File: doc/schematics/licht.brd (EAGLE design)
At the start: 49.5 x 40.3 mm, 16 parts, among them Q1 MOSFET-NCHANNELFDS6630A, X1 MKDSN1,5/2-5,08, X2 MKDSN1,5/2-5,08, X3 MKDSN1,5/2-5,08, X4 MKDSN1,5/2-5,08

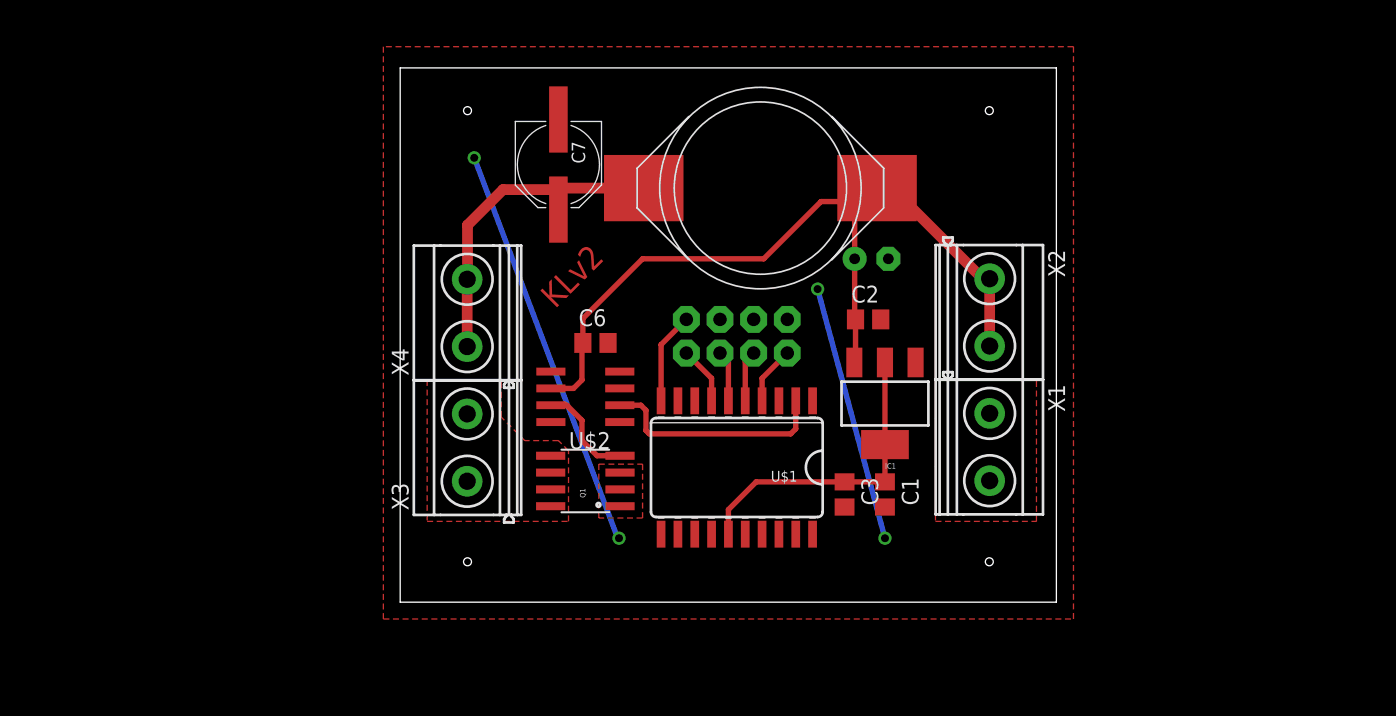
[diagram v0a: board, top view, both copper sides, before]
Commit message: Switched layout and board.
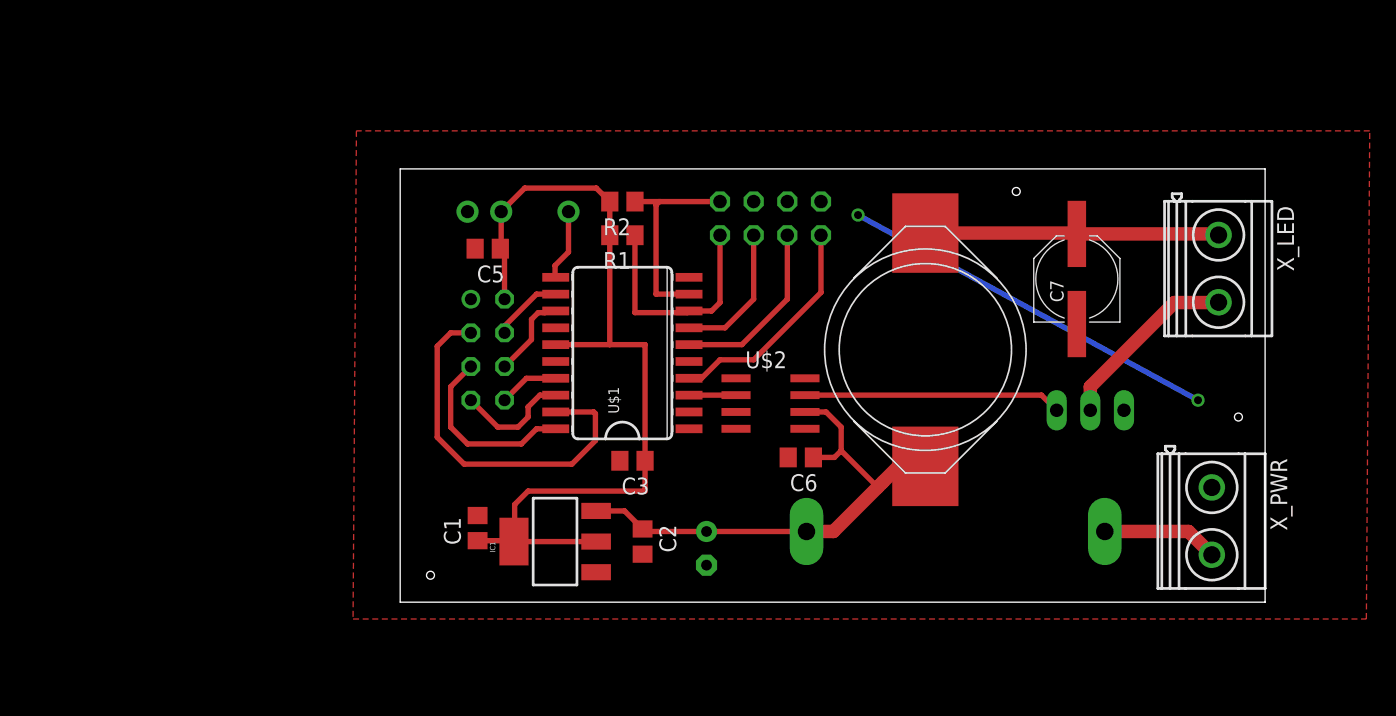
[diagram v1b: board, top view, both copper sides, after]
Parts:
- removed X1, X2, X3, X4: MKDSN1,5/2-5,08, con-phoenix-508:MKDSN1,5/2-5,08
- added C5: 100n, rcl:C0805
- added F1: (no value), fuse:SH22,5
- added IR1: TSOP1736TB1, tsop1736:TSOP17_TB1
- added NRF: (no value), florolf:FE04-2
- added R1, R2: 10k, rcl:R0805
- added X_LED, X_PWR: MKDSN1,5/2-5,08, con-phoenix-508:MKDSN1,5/2-5,08
- Q1: value MOSFET-NCHANNELFDS6630A -> MOSFET-NCHANNELFQP30N06L; device SparkFun-DiscreteSemi:SO08 -> SparkFun-DiscreteSemi:TO220V
- moved C7 40.1 mm to (51.1, 24.4), turned to 90 degrees
- moved Q1 38.5 mm to (52.1, 14.5), flipped to the bottom, turned to 180 degrees
- moved C1 30.8 mm to (5.84, 5.59), turned to 90 degrees
- moved IC1 27.0 mm to (11.7, 4.57), turned to 90 degrees
- moved C4 25.1 mm to (23.1, 4.06), turned to 270 degrees
- moved C2 23.9 mm to (18.3, 4.57), turned to 270 degrees
- moved C6 17.7 mm to (30.2, 10.9), turned to 180 degrees
- moved L1 17.4 mm to (39.6, 19.1), turned to 90 degrees
- moved C3 16.2 mm to (17.5, 10.7), turned to 180 degrees
- moved U$2 14.0 mm to (27.9, 15.0), turned to 270 degrees
- moved U$1 12.2 mm to (16.8, 18.8), turned to 90 degrees
- moved SV1 9.25 mm to (27.9, 29.0)
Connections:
- removed net MISC: SV1.8, U$1.10
- removed net OUT: Q1.5, Q1.6, Q1.7, Q1.8, X3.1, X3.2
- new net CE: NRF.3, U$1.19
- new net CSN: NRF.4, U$1.12
- new net IROUT: IR1.VO, U$1.11
- new net IRQ: NRF.8, U$1.17
- new net MISO: NRF.7, U$1.18
- new net MOSI: NRF.6, U$1.13
- new net N$2: Q1.2, X_LED.2
- new net N$3: F1.2, X_PWR.2
- new net ROT1: R2.1, SV1.8, U$1.9
- new net ROT2: R1.1, SV1.7, U$1.8
- new net SCK: NRF.5, U$1.20
- net +12V: now also F1.1; no longer X2.1, X2.2
- net +3V3: now also C5.1, IR1.VS, NRF.2, R1.2, R2.2
- net FET1: now also Q1.1; no longer Q1.4
- net GND: now also C5.2, IR1.GND, NRF.1, X_PWR.1; no longer Q1.1, Q1.2, X1.1, X1.2
- net N$1: now also X_LED.1; no longer X4.1, X4.2
- net PWM1: now also U$1.3; no longer U$1.2
- net SWCLK: now also SV1.3; no longer SV1.5
- net SWDIO: now also SV1.5; no longer SV1.7
- net WAKE: no longer SV1.3
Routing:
- net +3V3: track 23.5 -> 67.3 mm
- net CE: track 0.00 -> 28.4 mm
- net +12V: track 62.7 -> 38.7 mm
- net GND: track 50.4 -> 29.2 mm, vias 4 -> 2
- net ROT2: track 0.00 -> 17.7 mm
- net ROT1: track 0.00 -> 16.0 mm
- net SCK: track 0.00 -> 14.1 mm
- net N$2: track 0.00 -> 14.1 mm
- net PWM1: track 17.3 -> 3.55 mm
- net RST: track 4.40 -> 17.0 mm
- net FET1: track 7.69 -> 19.5 mm
- net SWCLK: track 3.87 -> 13.7 mm
- net N$3: track 0.00 -> 8.80 mm
- net MISO: track 0.00 -> 8.69 mm
- net MISC: track 6.94 -> 0.00 mm
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- removed copper zone on layer 1, net OUT
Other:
- board size 49.5 x 40.3 mm -> 65.3 x 32.7 mm
- board text removed: "KLv2"

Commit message: +Verpolungsschutz
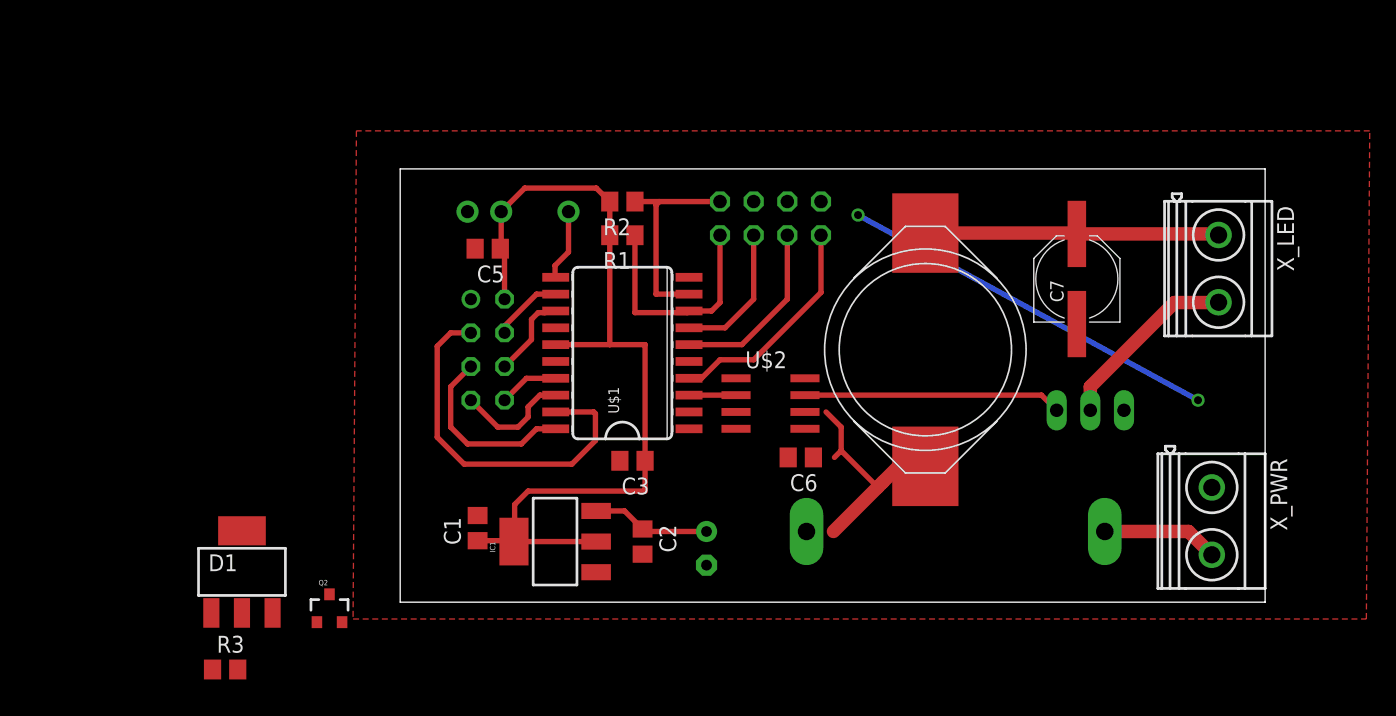
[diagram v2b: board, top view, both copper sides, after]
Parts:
- added D1: (no value), diode:SOT223
- added Q2: MOSFET-PCHANNELSMD, SparkFun-DiscreteSemi:SOT23-3
- added R3: 100k, rcl:R0805
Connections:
- new net N$4: F1.1, Q2.3
- new net N$5: D1.1, Q2.1, R3.2
- new net V+: C2.1, C4.+, C6.1, D1.4, IC1.3, Q2.2, U$2.6
- net +12V: no longer C2.1, C4.+, C6.1, F1.1, IC1.3, U$2.6
- net GND: now also R3.1
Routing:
- net +12V: track 38.7 -> 17.0 mm
- net V+: track 0.00 -> 8.97 mm
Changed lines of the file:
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@@
 <layer number="97" name="Info" color="7" fill="1" visible="no" active="no"/>
 <layer number="98" name="Guide" color="6" fill="1" visible="no" active="no"/>
+<layer number="99" name="SpiceOrder" color="5" fill="1" visible="no" active="no"/>
 <layer number="100" name="Muster" color="7" fill="1" visible="yes" active="yes"/>
 <layer number="101" name="Patch_Top" color="12" fill="4" visible="yes" active="yes"/>
@@
 <wire x1="65.258" y1="32.69" x2="0" y2="32.69" width="0" layer="20"/>
 <wire x1="0" y1="32.69" x2="0" y2="0" width="0" layer="20"/>
-<hole x="2.286" y="2.032" drill="0.6"/>
-<hole x="46.482" y="30.988" drill="0.6"/>
-<hole x="63.246" y="13.97" drill="0.6"/>
 </plain>
 <attributes>
@@
 <attribute name="OC_FARNELL" value="1162740" x="41.91" y="5.334" size="1.778" layer="28" font="vector" rot="MR180" display="off"/>
 </element>
+<element name="Q2" library="SparkFun-DiscreteSemi" package="SOT23-3" value="MOSFET-PCHANNELSMD" x="-5.334" y="-0.508"/>
+<element name="D1" library="diode" package="SOT223" value="" x="-11.938" y="2.286"/>
+<element name="R3" library="rcl" package="R0805" value="100k" x="-13.208" y="-5.08"/>
 </elements>
 <signals>
@@
 <via x="60.198" y="15.24" extent="1-16" drill="0.6"/>
 <wire x1="34.544" y1="29.21" x2="60.198" y2="15.24" width="0.4064" layer="16"/>
+<contactref element="R3" pad="1"/>
+<wire x1="5.842" y1="6.538" x2="-14.158" y2="-5.08" width="0" layer="19" extent="1-1"/>
 </signal>
 <signal name="+3V3">
@@
 </signal>
 <signal name="+12V">
-<contactref element="U$2" pad="6"/>
-<contactref element="C6" pad="1"/>
 <contactref element="L1" pad="1"/>
-<wire x1="30.54" y1="14.351" x2="32.131" y2="14.351" width="0.4064" layer="1"/>
 <wire x1="32.131" y1="14.351" x2="33.274" y2="13.208" width="0.4064" layer="1"/>
 <wire x1="33.274" y1="13.208" x2="33.274" y2="11.43" width="0.4064" layer="1"/>
 <wire x1="33.274" y1="11.43" x2="32.766" y2="10.922" width="0.4064" layer="1"/>
-<wire x1="32.766" y1="10.922" x2="31.176" y2="10.922" width="0.4064" layer="1"/>
-<contactref element="IC1" pad="3"/>
-<contactref element="C2" pad="1"/>
-<contactref element="C4" pad="+"/>
-<wire x1="18.288" y1="5.522" x2="18.476" y2="5.334" width="0.4064" layer="1"/>
-<contactref element="F1" pad="1"/>
-<wire x1="14.7828" y1="6.8834" x2="16.9266" y2="6.8834" width="0.4064" layer="1"/>
-<wire x1="16.9266" y1="6.8834" x2="18.288" y2="5.522" width="0.4064" layer="1"/>
-<wire x1="18.476" y1="5.334" x2="23.114" y2="5.334" width="0.4064" layer="1"/>
 <wire x1="36.0299" y1="8.6741" x2="36.4109" y2="9.0551" width="1.016" layer="1"/>
 <wire x1="36.4109" y1="9.0551" x2="37.6058" y2="10.25" width="1.016" layer="1"/>
 <wire x1="37.6058" y1="10.25" x2="39.624" y2="10.25" width="1.016" layer="1"/>
 <wire x1="33.274" y1="11.43" x2="36.0299" y2="8.6741" width="0.4064" layer="1"/>
-<wire x1="23.114" y1="5.334" x2="30.6578" y2="5.334" width="0.4064" layer="1"/>
-<wire x1="30.6578" y1="5.334" x2="32.6898" y2="5.334" width="1.016" layer="1"/>
 <wire x1="32.6898" y1="5.334" x2="36.0299" y2="8.6741" width="1.016" layer="1"/>
 </signal>
@@
 <wire x1="59.4821" y1="5.334" x2="61.239" y2="3.5771" width="1.016" layer="1"/>
 </signal>
+<signal name="N$4">
+<contactref element="F1" pad="1"/>
+<contactref element="Q2" pad="3"/>
+<wire x1="-5.334" y1="0.592" x2="30.6578" y2="5.334" width="0" layer="19" extent="1-1"/>
+</signal>
+<signal name="V+">
+<contactref element="IC1" pad="3"/>
+<contactref element="C2" pad="1"/>
+<contactref element="C4" pad="+"/>
+<wire x1="18.288" y1="5.522" x2="18.476" y2="5.334" width="0.4064" layer="1"/>
+<wire x1="14.7828" y1="6.8834" x2="16.9266" y2="6.8834" width="0.4064" layer="1"/>
+<wire x1="16.9266" y1="6.8834" x2="18.288" y2="5.522" width="0.4064" layer="1"/>
+<wire x1="18.476" y1="5.334" x2="23.114" y2="5.334" width="0.4064" layer="1"/>
+<contactref element="U$2" pad="6"/>
+<contactref element="C6" pad="1"/>
+<contactref element="Q2" pad="2"/>
+<contactref element="D1" pad="4"/>
+<wire x1="31.176" y1="10.922" x2="30.54" y2="14.351" width="0" layer="19" extent="1-1"/>
+<wire x1="23.114" y1="5.334" x2="31.176" y2="10.922" width="0" layer="19" extent="1-1"/>
+<wire x1="-4.384" y1="-1.508" x2="14.7828" y2="6.8834" width="0" layer="19" extent="1-1"/>
+<wire x1="-11.938" y1="5.385" x2="-4.384" y2="-1.508" width="0" layer="19" extent="1-1"/>
+</signal>
+<signal name="N$5">
+<contactref element="Q2" pad="1"/>
+<contactref element="D1" pad="1"/>
+<contactref element="R3" pad="2"/>
+<wire x1="-14.249" y1="-0.813" x2="-12.258" y2="-5.08" width="0" layer="19" extent="1-1"/>
+<wire x1="-6.284" y1="-1.508" x2="-12.258" y2="-5.08" width="0" layer="19" extent="1-1"/>
+</signal>
 </signals>

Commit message: pinheader geändert, reichelt-kompatiblen sicherungshalter
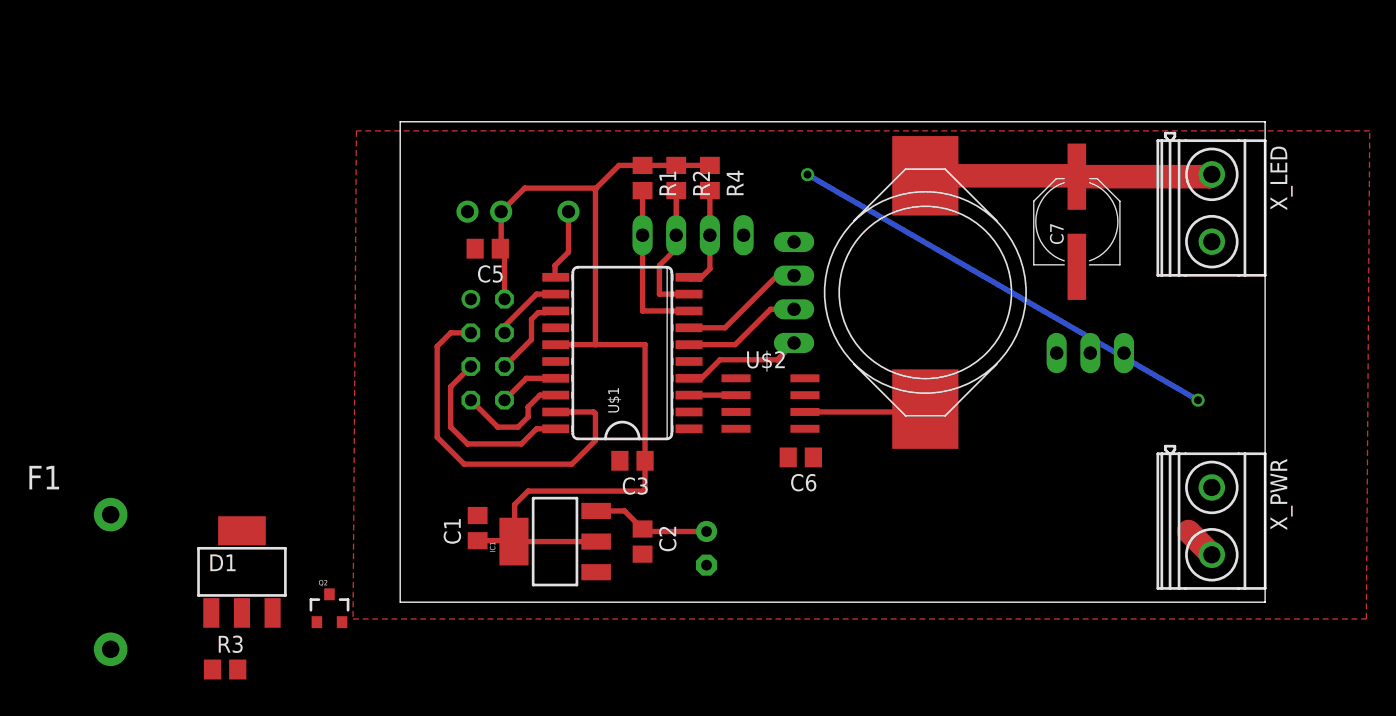
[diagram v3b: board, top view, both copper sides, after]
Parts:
- removed SV1: (no value), con-lstb:MA04-2
- added ISP, ROTARY: (no value), con-lstb:MA04-1
- added R4: 10k, rcl:R0805
- F1: device fuse:SH22,5 -> sprawl:PTF45
- moved F1 63.9 mm to (-21.8, 1.52), flipped to the top, turned to 0 degrees
- moved X_LED 4.60 mm to (61.2, 29.7)
- moved R1 4.58 mm to (18.3, 32.0), turned to 270 degrees
- moved R2 4.44 mm to (20.8, 32.0), turned to 270 degrees
- moved C7 4.32 mm to (51.1, 28.7)
- moved Q1 4.32 mm to (52.1, 18.8)
- moved L1 4.32 mm to (39.6, 23.4)
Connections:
- removed net +12V: L1.1
- new net ROTBTN: R4.2, ROTARY.2, U$1.10
- net +3V3: now also R1.1, R2.1, R4.1; no longer R1.2, R2.2
- net GND: now also ISP.1, ROTARY.1; no longer SV1.2, SV1.4, SV1.6
- net N$3: now also F1.1; no longer F1.2
- net N$4: now also F1.2; no longer F1.1
- net ROT1: now also R2.2, ROTARY.3; no longer R2.1, SV1.8
- net ROT2: now also R1.2, ROTARY.4; no longer R1.1, SV1.7
- net RST: now also ISP.4; no longer SV1.1
- net SWCLK: now also ISP.3; no longer SV1.3
- net SWDIO: now also ISP.2; no longer SV1.5
- net V+: now also L1.1
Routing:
- net FET1: track 19.5 -> 0.00 mm
- net +12V: track 17.0 -> 0.00 mm
- net N$2: track 14.1 -> 0.00 mm
- net V+: track 8.97 -> 18.1 mm
- net +3V3: track 67.3 -> 76.1 mm
- net RST: track 17.0 -> 9.03 mm
- net ROTBTN: track 0.00 -> 7.85 mm
- net N$3: track 8.80 -> 2.48 mm
- net ROT1: track 16.0 -> 10.6 mm
- net ROT2: track 17.7 -> 12.6 mm
- net GND: track 29.2 -> 34.0 mm
- net SWCLK: track 13.7 -> 9.03 mm
- net SWDIO: track 10.6 -> 9.56 mm
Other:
- board size 65.3 x 32.7 mm -> 65.3 x 36.2 mm
